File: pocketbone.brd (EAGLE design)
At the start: 55 x 35 mm, 61 parts, among them J1 USD_CONNECTOR, U1 24LC_32AT-I/OT, U2 OSD3358, U3 SN74LVC1G07_DCK_5, Y1 445C33D24M00000, Y2 CM200C-32.768KAZF-UT

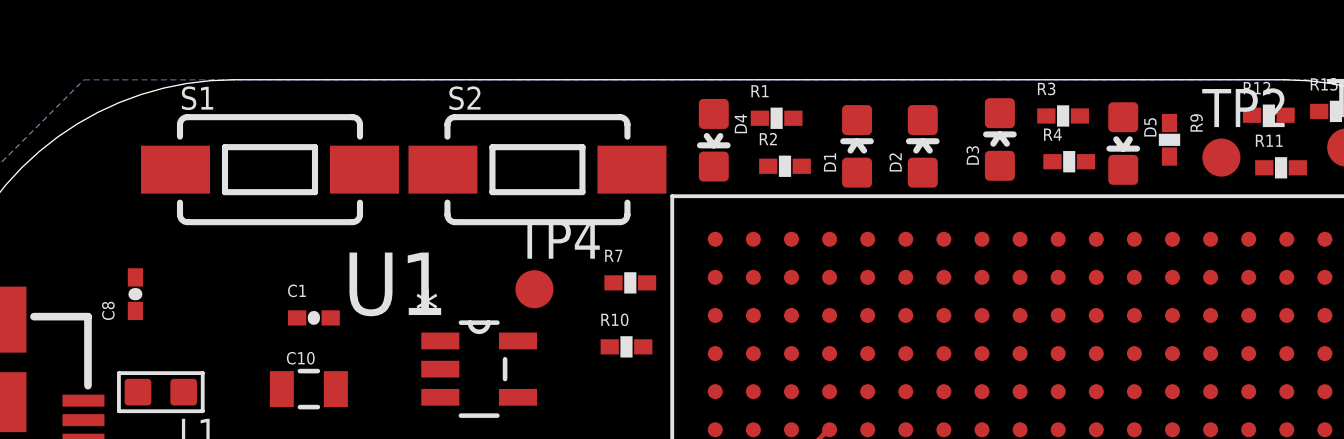
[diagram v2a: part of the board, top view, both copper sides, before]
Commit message: Update some ref designators
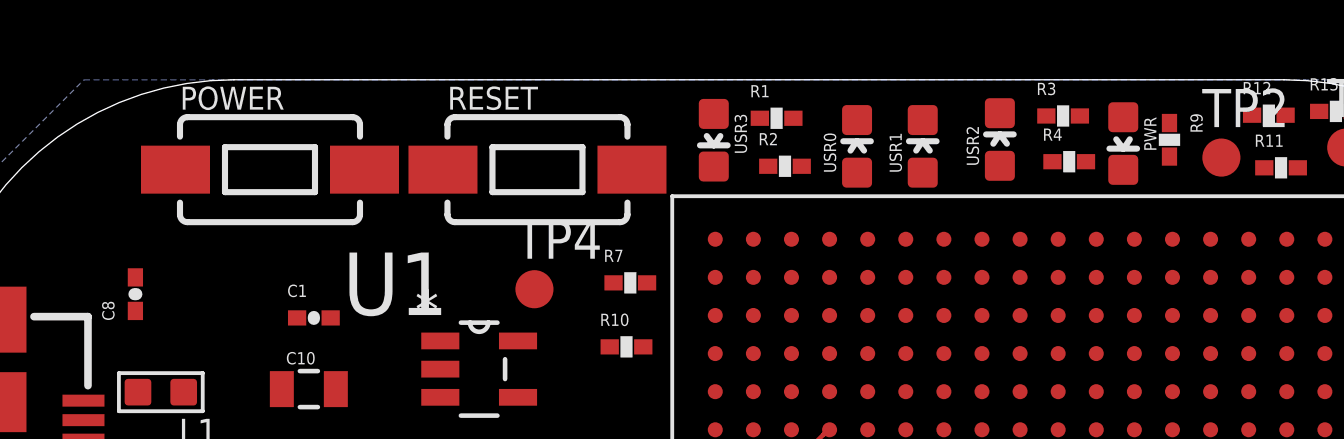
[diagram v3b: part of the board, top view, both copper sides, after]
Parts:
- Y1: value 445C33D24M00000 -> CM200C-32.768KAZF-UT; device pocketbone:445C33D24M00000 -> pocketbone:CM200C-32.768KAZF-UT
- Y2: value CM200C-32.768KAZF-UT -> 445C33D24M00000; device pocketbone:CM200C-32.768KAZF-UT -> pocketbone:445C33D24M00000
- moved Y1 11.0 mm to (16.0, 15.7), turned to 0 degrees
- moved Y2 11.0 mm to (25.2, 9.64), turned to 90 degrees
- renumbered D1 to USR0, D2 to USR1, D3 to USR2, D4 to USR3, D5 to PWR, S1 to POWER, S2 to RESET
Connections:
- net N$26: now also Y1.2; no longer Y2.2
- net N$27: now also Y1.1; no longer Y2.1
- net N$32: now also Y2.2; no longer Y1.2
- net N$33: now also Y2.1; no longer Y1.1
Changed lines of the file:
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@@
 <element name="C11" library="Strawson_Eagle_Lib" package="0402-CAP" value="0.1uF" x="10.5156" y="21.4884" rot="R180"/>
 <element name="C10" library="Strawson_Eagle_Lib" package="0805" value="10uF" x="12.4968" y="24.6888"/>
-<element name="D1" library="BeagleBone_Blue" package="LED-0603" value="BLUE" x="30.77" y="32.78"/>
-<element name="D2" library="BeagleBone_Blue" package="LED-0603" value="BLUE" x="32.96" y="32.78"/>
-<element name="D3" library="BeagleBone_Blue" package="LED-0603" value="BLUE" x="35.531" y="33.0086"/>
-<element name="D4" library="BeagleBone_Blue" package="LED-0603" value="BLUE" x="25.9948" y="32.9842" rot="R180"/>
-<element name="D5" library="BeagleBone_Blue" package="LED-0603" value="BLUE" x="39.6434" y="32.8744" rot="R180"/>
+<element name="USR0" library="BeagleBone_Blue" package="LED-0603" value="BLUE" x="30.77" y="32.78"/>
+<element name="USR1" library="BeagleBone_Blue" package="LED-0603" value="BLUE" x="32.96" y="32.78"/>
+<element name="USR2" library="BeagleBone_Blue" package="LED-0603" value="BLUE" x="35.531" y="33.0086"/>
+<element name="USR3" library="BeagleBone_Blue" package="LED-0603" value="BLUE" x="25.9948" y="32.9842" rot="R180"/>
+<element name="PWR" library="BeagleBone_Blue" package="LED-0603" value="BLUE" x="39.6434" y="32.8744" rot="R180"/>
 <element name="J1" library="pocketbone" package="MICRO-SD-SOCKET-PP" value="USD_CONNECTOR" x="6.7098" y="15.9898" rot="R180">
 <attribute name="PROD_ID" value="CONN-07820" x="6.7098" y="15.9898" size="1.778" layer="27" rot="R180" display="off"/>
@@
 <element name="JP2" library="pocketbone" package="USB-AB-MICRO-SMD" value="USB-MICRO-SMD" x="2.09" y="12.1372"/>
 <element name="JP1" library="pocketbone" package="USB-AB-MICRO-SMD" value="USB-MICRO-SMD" x="2.134" y="23.0042"/>
-<element name="Y2" library="pocketbone" package="CM200C-32.768KAZF-UT" value="CM200C-32.768KAZF-UT" x="15.999" y="15.658"/>
-<element name="Y1" library="pocketbone" package="445C33D24M00000" value="445C33D24M00000" x="25.1948" y="9.636" rot="R90"/>
+<element name="Y1" library="pocketbone" package="CM200C-32.768KAZF-UT" value="CM200C-32.768KAZF-UT" x="15.999" y="15.658"/>
+<element name="Y2" library="pocketbone" package="445C33D24M00000" value="445C33D24M00000" x="25.1948" y="9.636" rot="R90"/>
 <element name="TP3" library="testpad" package="B1,27" value="TPSQB1,27" x="4.191" y="4.4958">
 <attribute name="TP_SIGNAL_NAME" value="GND" x="4.191" y="4.4958" size="1.778" layer="27" display="off"/>
 </element>
-<element name="S1" library="SparkFun-Electromechanical" package="TACTILE-SWITCH-1101NE" value="SWITCH-MOMENTARY-2SMD-1101NE" x="11.2014" y="32.004">
+<element name="POWER" library="SparkFun-Electromechanical" package="TACTILE-SWITCH-1101NE" value="SWITCH-MOMENTARY-2SMD-1101NE" x="11.2014" y="32.004">
 <attribute name="PROD_ID" value="SWCH-00815" x="11.2014" y="32.004" size="1.778" layer="27" display="off"/>
 </element>
-<element name="S2" library="SparkFun-Electromechanical" package="TACTILE-SWITCH-1101NE" value="SWITCH-MOMENTARY-2SMD-1101NE" x="20.1168" y="32.004">
+<element name="RESET" library="SparkFun-Electromechanical" package="TACTILE-SWITCH-1101NE" value="SWITCH-MOMENTARY-2SMD-1101NE" x="20.1168" y="32.004">
 <attribute name="PROD_ID" value="SWCH-00815" x="20.1168" y="32.004" size="1.778" layer="27" display="off"/>
 </element>
@@
 <signal name="PWR">
 <contactref element="U2" pad="D20"/>
-<contactref element="S1" pad="2"/>
+<contactref element="POWER" pad="2"/>
 <wire x1="26.0444" y1="9.3632" x2="14.3514" y2="32.004" width="0" layer="19" extent="1-1"/>
 </signal>
@@
 <signal name="VDD_3V3AUX">
 <contactref element="U2" pad="Y11"/>
-<contactref element="D5" pad="A"/>
+<contactref element="PWR" pad="A"/>
 <wire x1="37.4744" y1="29.6832" x2="39.6434" y2="33.7514" width="0" layer="19" extent="1-1"/>
 </signal>
 <signal name="PWR_LEDR">
-<contactref element="D5" pad="C"/>
+<contactref element="PWR" pad="C"/>
 <contactref element="R9" pad="1"/>
 <wire x1="39.6434" y1="31.9974" x2="41.184259375" y2="33.5572" width="0" layer="19" extent="1-1"/>
@@
 <contactref element="R29" pad="2"/>
 <contactref element="TP3" pad="TP"/>
-<contactref element="S2" pad="1"/>
-<contactref element="S1" pad="1"/>
+<contactref element="RESET" pad="1"/>
+<contactref element="POWER" pad="1"/>
 <polygon width="0.1524" layer="16">
 <vertex x="10" y="0"/>
@@
 </signal>
 <signal name="N$26">
-<contactref element="Y2" pad="2"/>
+<contactref element="Y1" pad="2"/>
 <contactref element="C7" pad="1"/>
 <contactref element="U2" pad="M20"/>
@@
 <signal name="N$27">
 <contactref element="U2" pad="K20"/>
-<contactref element="Y2" pad="1"/>
+<contactref element="Y1" pad="1"/>
 <contactref element="C5" pad="1"/>
 <wire x1="26.0444" y1="16.9832" x2="24.0792" y2="19.4818" width="0.1524" layer="1"/>
@@
 <contactref element="U2" pad="H20"/>
 <contactref element="C6" pad="1"/>
-<contactref element="Y1" pad="2"/>
+<contactref element="Y2" pad="2"/>
 <wire x1="26.0444" y1="14.4432" x2="22.9176" y2="14.4432" width="0.1524" layer="1"/>
 <wire x1="22.9176" y1="14.4432" x2="22.6548" y2="14.706" width="0.1524" layer="1"/>
@@
 <contactref element="U2" pad="F20"/>
 <contactref element="C4" pad="2"/>
-<contactref element="Y1" pad="1"/>
+<contactref element="Y2" pad="1"/>
 <wire x1="22.6548" y1="10.906" x2="25.0472" y2="10.906" width="0.1524" layer="1"/>
 <wire x1="25.0472" y1="10.906" x2="26.0444" y2="11.9032" width="0.1524" layer="1"/>
@@
 <contactref element="C9" pad="1"/>
 <contactref element="U3" pad="4"/>
-<contactref element="S2" pad="2"/>
+<contactref element="RESET" pad="2"/>
 <wire x1="22.526" y1="26.096659375" x2="23.2668" y2="32.004" width="0" layer="19" extent="1-1"/>
 <wire x1="38.7444" y1="5.5532" x2="22.526" y2="26.096659375" width="0" layer="19" extent="1-1"/>
@@
 <signal name="N$43">
 <contactref element="U2" pad="V16"/>
-<contactref element="D4" pad="A"/>
+<contactref element="USR3" pad="A"/>
 <wire x1="31.1244" y1="27.1432" x2="25.9948" y2="33.8612" width="0" layer="19" extent="1-1"/>
 </signal>
 <signal name="N$44">
 <contactref element="U2" pad="T15"/>
-<contactref element="D3" pad="A"/>
+<contactref element="USR2" pad="A"/>
 <wire x1="32.3944" y1="24.6032" x2="35.531" y2="32.1316" width="0" layer="19" extent="1-1"/>
 </signal>
 <signal name="N$45">
 <contactref element="U2" pad="U15"/>
-<contactref element="D2" pad="A"/>
+<contactref element="USR1" pad="A"/>
 <wire x1="32.3944" y1="25.8732" x2="32.96" y2="31.903" width="0" layer="19" extent="1-1"/>
 </signal>
 <signal name="N$46">
 <contactref element="U2" pad="V15"/>
-<contactref element="D1" pad="A"/>
+<contactref element="USR0" pad="A"/>
 <wire x1="32.3944" y1="27.1432" x2="30.77" y2="31.903" width="0" layer="19" extent="1-1"/>
 </signal>
 <signal name="N$47">
-<contactref element="D1" pad="C"/>
+<contactref element="USR0" pad="C"/>
 <contactref element="R1" pad="2"/>
 <wire x1="28.6474" y1="33.716659375" x2="30.77" y2="33.657" width="0" layer="19" extent="1-1"/>
 </signal>
 <signal name="N$57">
-<contactref element="D2" pad="C"/>
+<contactref element="USR1" pad="C"/>
 <contactref element="R2" pad="2"/>
 <wire x1="28.9268" y1="32.116459375" x2="32.96" y2="33.657" width="0" layer="19" extent="1-1"/>
 </signal>
 <signal name="N$58">
-<contactref element="D3" pad="C"/>
+<contactref element="USR2" pad="C"/>
 <contactref element="R3" pad="2"/>
 <wire x1="35.531" y1="33.8856" x2="38.1978" y2="33.792859375" width="0" layer="19" extent="1-1"/>
 </signal>
 <signal name="N$59">
-<contactref element="D4" pad="C"/>
+<contactref element="USR3" pad="C"/>
 <contactref element="R4" pad="2"/>
 <wire x1="25.9948" y1="32.1072" x2="38.401" y2="32.268859375" width="0" layer="19" extent="1-1"/>

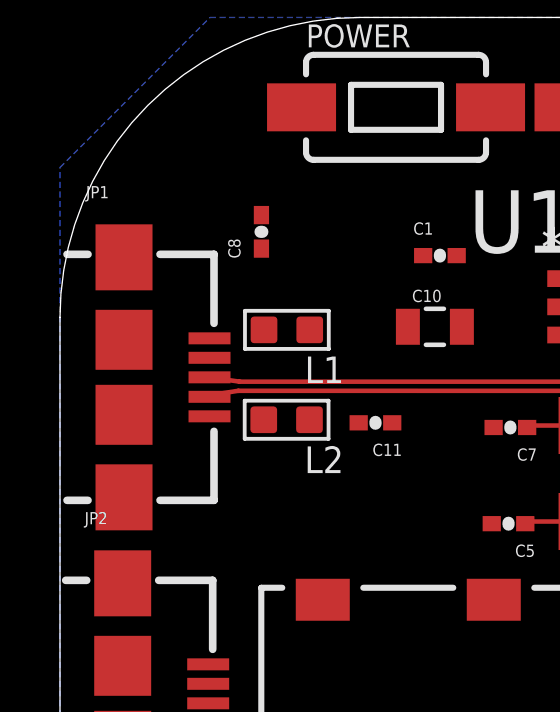
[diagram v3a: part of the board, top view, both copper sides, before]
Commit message: Rename USB connectors
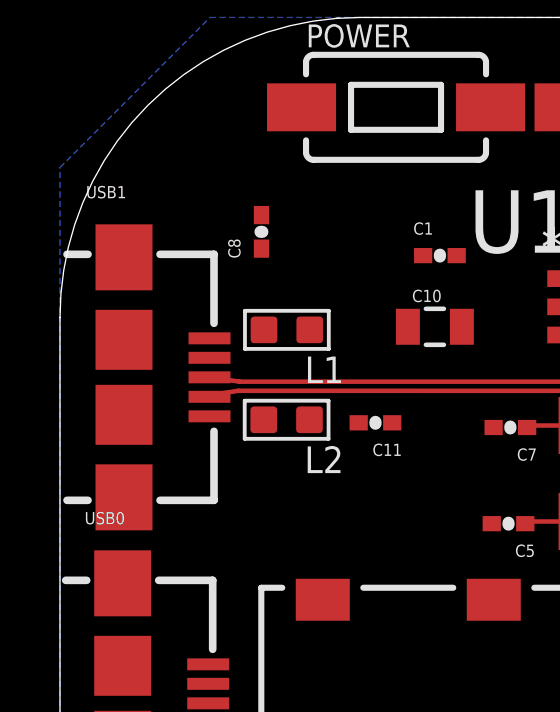
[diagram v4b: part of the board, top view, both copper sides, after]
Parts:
- renumbered JP1 to USB1, JP2 to USB0
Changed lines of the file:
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@@
 <attribute name="DESCRIPTION" value="Single Buffer/Driver With Open-Drain Output" x="32.1146" y="2.4178" size="1.778" layer="27" display="off"/>
 </element>
-<element name="JP2" library="pocketbone" package="USB-AB-MICRO-SMD" value="USB-MICRO-SMD" x="2.09" y="12.1372"/>
-<element name="JP1" library="pocketbone" package="USB-AB-MICRO-SMD" value="USB-MICRO-SMD" x="2.134" y="23.0042"/>
+<element name="USB0" library="pocketbone" package="USB-AB-MICRO-SMD" value="USB-MICRO-SMD" x="2.09" y="12.1372"/>
+<element name="USB1" library="pocketbone" package="USB-AB-MICRO-SMD" value="USB-MICRO-SMD" x="2.134" y="23.0042"/>
 <element name="Y1" library="pocketbone" package="CM200C-32.768KAZF-UT" value="CM200C-32.768KAZF-UT" x="15.999" y="15.658"/>
 <element name="Y2" library="pocketbone" package="445C33D24M00000" value="445C33D24M00000" x="25.1948" y="9.636" rot="R90"/>
@@
 <contactref element="U2" pad="Y8"/>
 <contactref element="U2" pad="Y9"/>
-<contactref element="JP2" pad="VBUS"/>
+<contactref element="USB0" pad="VBUS"/>
 <contactref element="U2" pad="P15"/>
 <wire x1="40.0144" y1="29.6832" x2="41.2844" y2="29.6832" width="0" layer="19" extent="1-1"/>
@@
 <contactref element="C11" pad="2"/>
 <contactref element="C10" pad="2"/>
-<contactref element="JP2" pad="GND"/>
-<contactref element="JP2" pad="SHIELD1"/>
-<contactref element="JP2" pad="SHIELD2"/>
-<contactref element="JP2" pad="SHIELD3"/>
-<contactref element="JP2" pad="SHIELD4"/>
+<contactref element="USB0" pad="GND"/>
+<contactref element="USB0" pad="SHIELD1"/>
+<contactref element="USB0" pad="SHIELD2"/>
+<contactref element="USB0" pad="SHIELD3"/>
+<contactref element="USB0" pad="SHIELD4"/>
 <contactref element="U2" pad="A1"/>
 <contactref element="U2" pad="J6"/>
@@
 <signal name="USB0_DP" class="2">
 <contactref element="U2" pad="N17"/>
-<contactref element="JP2" pad="D+"/>
+<contactref element="USB0" pad="D+"/>
 <wire x1="4.94" y1="12.1372" x2="29.8544" y2="20.7932" width="0" layer="19" extent="1-1"/>
 </signal>
 <signal name="USB0_DM" class="2">
 <contactref element="U2" pad="N18"/>
-<contactref element="JP2" pad="D-"/>
+<contactref element="USB0" pad="D-"/>
 <wire x1="4.94" y1="12.7872" x2="28.5844" y2="20.7932" width="0" layer="19" extent="1-1"/>
 </signal>
 <signal name="USB0_ID">
 <contactref element="U2" pad="P16"/>
-<contactref element="JP2" pad="ID"/>
+<contactref element="USB0" pad="ID"/>
 <wire x1="4.94" y1="11.4872" x2="31.1244" y2="22.0632" width="0" layer="19" extent="1-1"/>
 </signal>
 <signal name="USB1_DP" class="2">
 <contactref element="U2" pad="R17"/>
-<contactref element="JP1" pad="D+"/>
+<contactref element="USB1" pad="D+"/>
 <wire x1="29.8544" y1="23.3332" x2="29.6578" y2="23.1808" width="0.1524" layer="1"/>
 <wire x1="29.6578" y1="23.1808" x2="29.337" y2="22.857459375" width="0.1524" layer="1"/>
@@
 <signal name="USB1_DM" class="2">
 <contactref element="U2" pad="R18"/>
-<contactref element="JP1" pad="D-"/>
+<contactref element="USB1" pad="D-"/>
 <wire x1="4.984" y1="23.6542" x2="28.5844" y2="23.3332" width="0" layer="19" extent="1-1"/>
 </signal>
 <signal name="N$128" class="3">
 <contactref element="L2" pad="2"/>
-<contactref element="JP1" pad="SHIELD1"/>
-<contactref element="JP1" pad="SHIELD2"/>
-<contactref element="JP1" pad="SHIELD3"/>
-<contactref element="JP1" pad="SHIELD4"/>
-<contactref element="JP1" pad="GND"/>
+<contactref element="USB1" pad="SHIELD1"/>
+<contactref element="USB1" pad="SHIELD2"/>
+<contactref element="USB1" pad="SHIELD3"/>
+<contactref element="USB1" pad="SHIELD4"/>
+<contactref element="USB1" pad="GND"/>
 <wire x1="4.984" y1="21.7042" x2="6.792" y2="21.5896" width="0" layer="19" extent="1-1"/>
 <wire x1="2.134" y1="21.7542" x2="4.984" y2="21.7042" width="0" layer="19" extent="1-1"/>
@@
 <signal name="USB1_ID">
 <contactref element="U2" pad="P17"/>
-<contactref element="JP1" pad="ID"/>
+<contactref element="USB1" pad="ID"/>
 <wire x1="29.8544" y1="22.0632" x2="29.829" y2="22.0632" width="0.1524" layer="1"/>
 <wire x1="29.829" y1="22.0632" x2="29.337" y2="22.552659375" width="0.1524" layer="1"/>
@@
 <signal name="N$1">
 <contactref element="L1" pad="2"/>
-<contactref element="JP1" pad="VBUS"/>
+<contactref element="USB1" pad="VBUS"/>
 <wire x1="4.984" y1="24.3042" x2="6.8006" y2="24.5864" width="0" layer="19" extent="1-1"/>
 </signal>
